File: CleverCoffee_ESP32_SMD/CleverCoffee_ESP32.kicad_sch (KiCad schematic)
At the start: 48 parts, among them Q1 2N7002, Q2 2N7002, Q3 2N7002, Q4 2N7002, Q5 2N7002

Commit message: Finalize DRC and add production files
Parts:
- B_SW1, DIMMER1, ESP1, E_TRIG1, F_SENS1, HT_RL1, I2C1, JP1, JTAG1, PV_RL1, P_SENS1, P_SW1, ROTARY1, SCALE1, S_LED1, S_SW1, T_SENS1, V_IN1, W_SENS1: JLCPCB BOM (none) -> false
- C1: JLCPCB BOM (none) -> false; LCSC C14663 -> (none)
- C2, C3, C4: JLCPCB BOM (none) -> true; LCSC C14663 -> (none); LCSC Part (none) -> C14663
- Q1, Q2, Q3, Q4, Q5: JLCPCB BOM (none) -> true; LCSC C8545 -> (none); LCSC Part (none) -> C8545
- R1, R2, R3: JLCPCB BOM (none) -> true; LCSC C23162 -> (none); LCSC Part (none) -> C23162
- R10, R16, R8: JLCPCB BOM (none) -> true; LCSC C22775 -> (none); LCSC Part (none) -> C22775
- R11, R12, R13, R4, R5, R9: JLCPCB BOM (none) -> true; LCSC C25819 -> (none); LCSC Part (none) -> C25819
- R14, R6, R7: JLCPCB BOM (none) -> true; LCSC C23179 -> (none); LCSC Part (none) -> C23179
- R15, R17, R19, R20: JLCPCB BOM (none) -> true; LCSC C25804 -> (none); LCSC Part (none) -> C25804
- R18: JLCPCB BOM (none) -> true; LCSC C22962 -> (none); LCSC Part (none) -> C22962

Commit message: Final touches and production files
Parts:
- Q1, Q2, Q3, Q4, Q5: JLCPCB Rotation Offset (none) -> 180

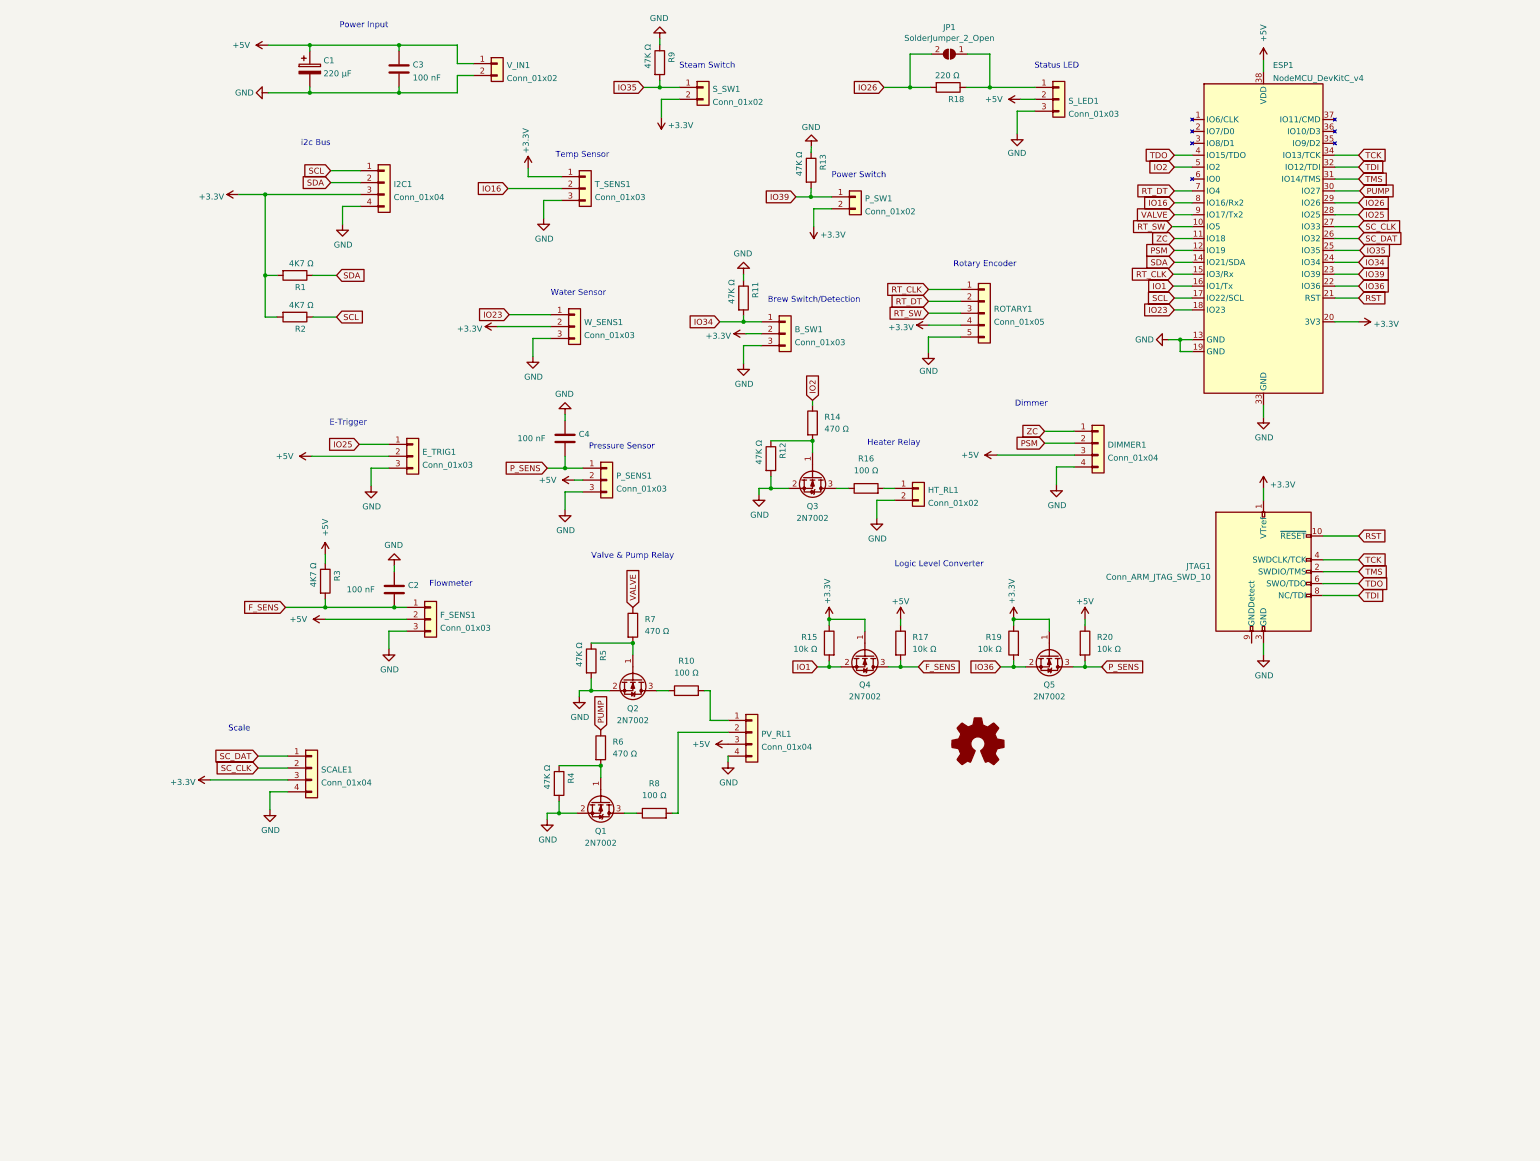
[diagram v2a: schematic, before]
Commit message: Adds SPICE model
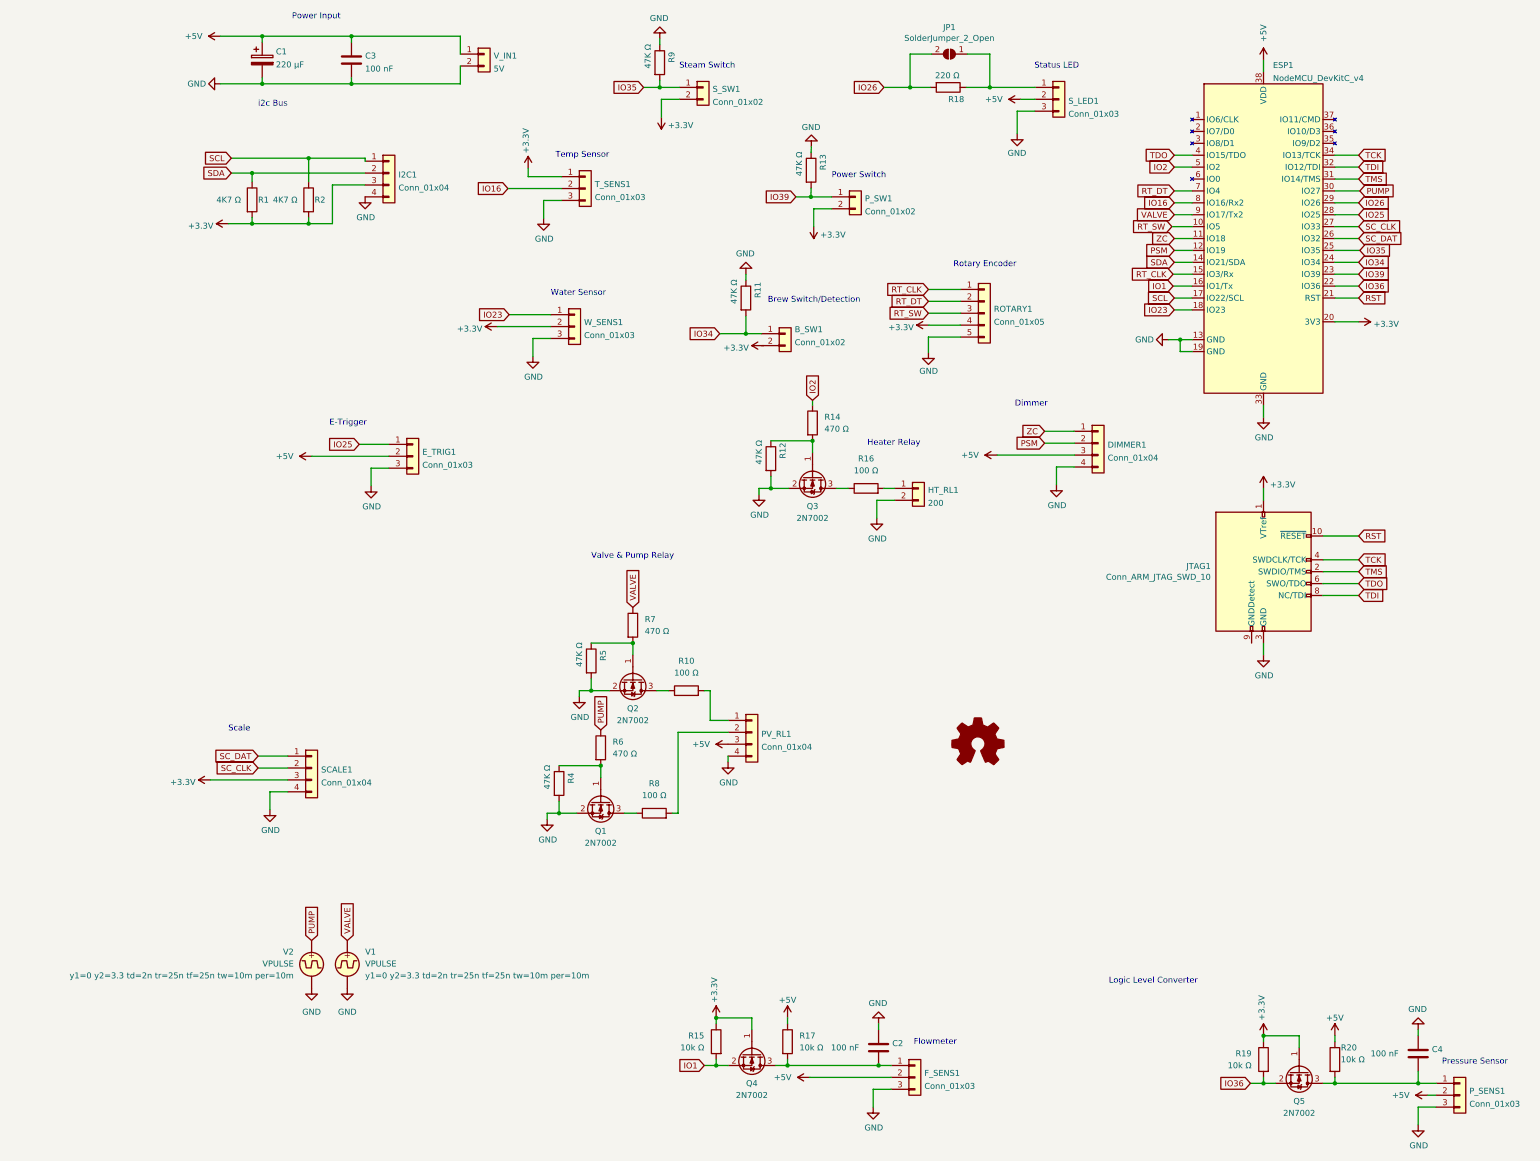
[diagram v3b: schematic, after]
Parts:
- removed R3: 4K7 Ω, Capacitor_SMD:C_0603_1608Metric, symbol Device:R
- added V1, V2: VPULSE, symbol Simulation_SPICE:VPULSE
- B_SW1: value Conn_01x03 -> Conn_01x02; footprint Connector_PinSocket_2.54mm:PinSocket_1x03_P2.54mm_Vertical -> Connector_PinSocket_2.54mm:PinSocket_1x02_P2.54mm_Vertical; symbol Connector_Generic:Conn_01x03 -> Connector_Generic:Conn_01x02
- HT_RL1: value Conn_01x02 -> 200
- V_IN1: value Conn_01x02 -> 5V
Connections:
- net +3V3: no longer B_SW1.2 (Pin_2)
- net GND: now also V1.2, V2.2; no longer B_SW1.3 (Pin_3)
- net PUMP: now also V2.1
- net VALVE: now also V1.1
- net F_SENS: no longer names the net of C2.2, F_SENS1.1 (Pin_1), Q4.3 (D), R17.2
- net P_SENS: no longer names the net of C4.2, P_SENS1.1 (Pin_1), Q5.3 (D), R20.2
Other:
- moved on the sheet: C1, C3, I2C1, R1, R11, R2, V_IN1
